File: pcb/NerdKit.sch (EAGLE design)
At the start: 30 parts, among them U2 ARDUINOR3-PINSONLY

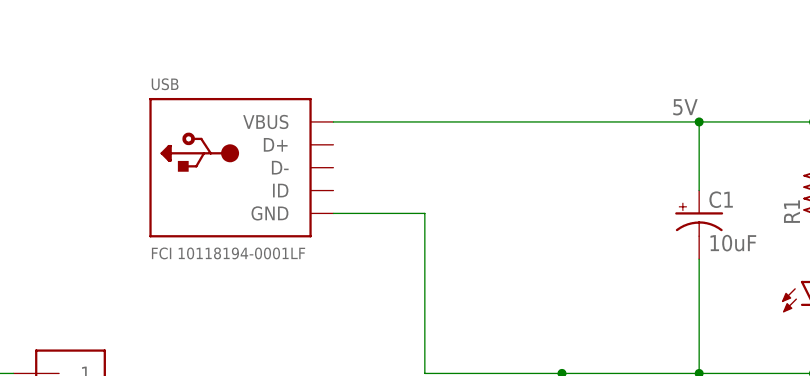
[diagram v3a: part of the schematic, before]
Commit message: Added mounting holes.
Also brought the USB D+ and D- signals out to test points, just for fun.
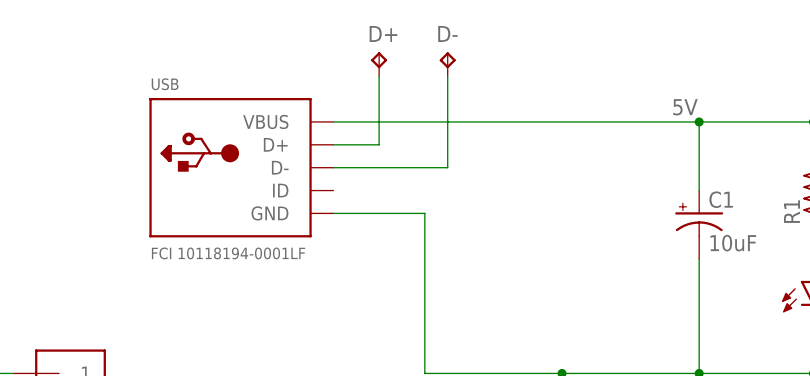
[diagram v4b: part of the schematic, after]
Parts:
- added D+, D-: TPPAD1-13, testpad:TPPAD1-13
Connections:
- new net N$2: D+.TP, USB.D+
- new net N$21: D-.TP, USB.D-
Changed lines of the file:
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@@
 <grid distance="0.1" unitdist="inch" unit="inch" style="lines" multiple="1" display="no" altdistance="0.01" altunitdist="inch" altunit="inch"/>
 <layers>
-<layer number="1" name="Top" color="4" fill="1" visible="no" active="no"/>
-<layer number="2" name="Route2" color="1" fill="3" visible="no" active="no"/>
-<layer number="3" name="Route3" color="4" fill="3" visible="no" active="no"/>
-<layer number="14" name="Route14" color="1" fill="6" visible="no" active="no"/>
-<layer number="15" name="Route15" color="4" fill="6" visible="no" active="no"/>
-<layer number="16" name="Bottom" color="1" fill="1" visible="no" active="no"/>
-<layer number="17" name="Pads" color="2" fill="1" visible="no" active="no"/>
-<layer number="18" name="Vias" color="2" fill="1" visible="no" active="no"/>
-<layer number="19" name="Unrouted" color="6" fill="1" visible="no" active="no"/>
-<layer number="20" name="Dimension" color="15" fill="1" visible="no" active="no"/>
-<layer number="21" name="tPlace" color="7" fill="1" visible="no" active="no"/>
-<layer number="22" name="bPlace" color="7" fill="1" visible="no" active="no"/>
-<layer number="23" name="tOrigins" color="15" fill="1" visible="no" active="no"/>
-<layer number="24" name="bOrigins" color="15" fill="1" visible="no" active="no"/>
-<layer number="25" name="tNames" color="7" fill="1" visible="no" active="no"/>
-<layer number="26" name="bNames" color="7" fill="1" visible="no" active="no"/>
-<layer number="27" name="tValues" color="7" fill="1" visible="no" active="no"/>
-<layer number="28" name="bValues" color="7" fill="1" visible="no" active="no"/>
+<layer number="1" name="Top" color="4" fill="1" visible="yes" active="no"/>
+<layer number="2" name="Route2" color="1" fill="3" visible="yes" active="no"/>
+<layer number="3" name="Route3" color="4" fill="3" visible="yes" active="no"/>
+<layer number="14" name="Route14" color="1" fill="6" visible="yes" active="no"/>
+<layer number="15" name="Route15" color="4" fill="6" visible="yes" active="no"/>
+<layer number="16" name="Bottom" color="1" fill="1" visible="yes" active="no"/>
+<layer number="17" name="Pads" color="2" fill="1" visible="yes" active="no"/>
+<layer number="18" name="Vias" color="2" fill="1" visible="yes" active="no"/>
+<layer number="19" name="Unrouted" color="6" fill="1" visible="yes" active="no"/>
+<layer number="20" name="Dimension" color="15" fill="1" visible="yes" active="no"/>
+<layer number="21" name="tPlace" color="7" fill="1" visible="yes" active="no"/>
+<layer number="22" name="bPlace" color="7" fill="1" visible="yes" active="no"/>
+<layer number="23" name="tOrigins" color="15" fill="1" visible="yes" active="no"/>
+<layer number="24" name="bOrigins" color="15" fill="1" visible="yes" active="no"/>
+<layer number="25" name="tNames" color="7" fill="1" visible="yes" active="no"/>
+<layer number="26" name="bNames" color="7" fill="1" visible="yes" active="no"/>
+<layer number="27" name="tValues" color="7" fill="1" visible="yes" active="no"/>
+<layer number="28" name="bValues" color="7" fill="1" visible="yes" active="no"/>
 <layer number="29" name="tStop" color="7" fill="3" visible="no" active="no"/>
 <layer number="30" name="bStop" color="7" fill="6" visible="no" active="no"/>
@@
 <layer number="35" name="tGlue" color="7" fill="4" visible="no" active="no"/>
 <layer number="36" name="bGlue" color="7" fill="5" visible="no" active="no"/>
-<layer number="37" name="tTest" color="7" fill="1" visible="no" active="no"/>
-<layer number="38" name="bTest" color="7" fill="1" visible="no" active="no"/>
+<layer number="37" name="tTest" color="7" fill="1" visible="yes" active="no"/>
+<layer number="38" name="bTest" color="7" fill="1" visible="yes" active="no"/>
 <layer number="39" name="tKeepout" color="4" fill="11" visible="no" active="no"/>
 <layer number="40" name="bKeepout" color="1" fill="11" visible="no" active="no"/>
@@
 <layer number="44" name="Drills" color="7" fill="1" visible="no" active="no"/>
 <layer number="45" name="Holes" color="7" fill="1" visible="no" active="no"/>
-<layer number="46" name="Milling" color="3" fill="1" visible="no" active="no"/>
-<layer number="47" name="Measures" color="7" fill="1" visible="no" active="no"/>
-<layer number="48" name="Document" color="7" fill="1" visible="no" active="no"/>
-<layer number="49" name="Reference" color="7" fill="1" visible="no" active="no"/>
-<layer number="50" name="dxf" color="7" fill="1" visible="no" active="no"/>
-<layer number="51" name="tDocu" color="7" fill="1" visible="no" active="no"/>
-<layer number="52" name="bDocu" color="7" fill="1" visible="no" active="no"/>
-<layer number="53" name="tGND_GNDA" color="7" fill="9" visible="no" active="no"/>
-<layer number="54" name="bGND_GNDA" color="1" fill="9" visible="no" active="no"/>
-<layer number="56" name="wert" color="7" fill="1" visible="no" active="no"/>
-<layer number="57" name="tCAD" color="7" fill="1" visible="no" active="no"/>
-<layer number="59" name="tCarbon" color="7" fill="1" visible="no" active="no"/>
-<layer number="60" name="bCarbon" color="7" fill="1" visible="no" active="no"/>
+<layer number="46" name="Milling" color="3" fill="1" visible="yes" active="no"/>
+<layer number="47" name="Measures" color="7" fill="1" visible="yes" active="no"/>
+<layer number="48" name="Document" color="7" fill="1" visible="yes" active="no"/>
+<layer number="49" name="Reference" color="7" fill="1" visible="yes" active="no"/>
+<layer number="50" name="dxf" color="7" fill="1" visible="yes" active="no"/>
+<layer number="51" name="tDocu" color="7" fill="1" visible="yes" active="no"/>
+<layer number="52" name="bDocu" color="7" fill="1" visible="yes" active="no"/>
+<layer number="53" name="tGND_GNDA" color="7" fill="9" visible="yes" active="no"/>
+<layer number="54" name="bGND_GNDA" color="1" fill="9" visible="yes" active="no"/>
+<layer number="56" name="wert" color="7" fill="1" visible="yes" active="no"/>
+<layer number="57" name="tCAD" color="7" fill="1" visible="yes" active="no"/>
+<layer number="59" name="tCarbon" color="7" fill="1" visible="yes" active="no"/>
+<layer number="60" name="bCarbon" color="7" fill="1" visible="yes" active="no"/>
 <layer number="90" name="Modules" color="5" fill="1" visible="yes" active="yes"/>
 <layer number="91" name="Nets" color="2" fill="1" visible="yes" active="yes"/>
@@
 <part name="ARDUINOIO1" library="pinhead" deviceset="PINHD-2X20" device=""/>
 <part name="USB" library="microbuilder" deviceset="USB" device="MICRO_20329" value="FCI 10118194-0001LF"/>
+<part name="D+" library="testpad" deviceset="TP" device="PAD1-13"/>
+<part name="D-" library="testpad" deviceset="TP" device="PAD1-13"/>
 </parts>
 <sheets>
@@
 <instance part="ARDUINOIO1" gate="A" x="25.4" y="-45.72"/>
 <instance part="USB" gate="G$1" x="45.72" y="91.44"/>
+<instance part="D+" gate="G$1" x="60.96" y="104.14"/>
+<instance part="D-" gate="G$1" x="68.58" y="104.14"/>
 </instances>
 <busses>
@@
 </segment>
 </net>
+<net name="N$2" class="0">
+<segment>
+<pinref part="USB" gate="G$1" pin="D+"/>
+<pinref part="D+" gate="G$1" pin="TP"/>
+<wire x1="55.88" y1="93.98" x2="60.96" y2="93.98" width="0.1524" layer="91"/>
+<wire x1="60.96" y1="93.98" x2="60.96" y2="101.6" width="0.1524" layer="91"/>
+</segment>
+</net>
+<net name="N$21" class="0">
+<segment>
+<pinref part="USB" gate="G$1" pin="D-"/>
+<pinref part="D-" gate="G$1" pin="TP"/>
+<wire x1="55.88" y1="91.44" x2="68.58" y2="91.44" width="0.1524" layer="91"/>
+<wire x1="68.58" y1="91.44" x2="68.58" y2="101.6" width="0.1524" layer="91"/>
+</segment>
+</net>
